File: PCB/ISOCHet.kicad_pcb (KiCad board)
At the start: 2 copper layers, 57.1 x 38.1 mm, 19 parts, among them J1 USB_C_Receptacle_USB2.0, J2 Conn_01x08_Pin, SW0 BOOT, SW1 TAB, SW2 ENTER, SW3 CAPS, SW4 CAPS_STEP1.5, SW5 CAPS_STEP1.25, U1 CH552G, U2 USBLC6-2P6

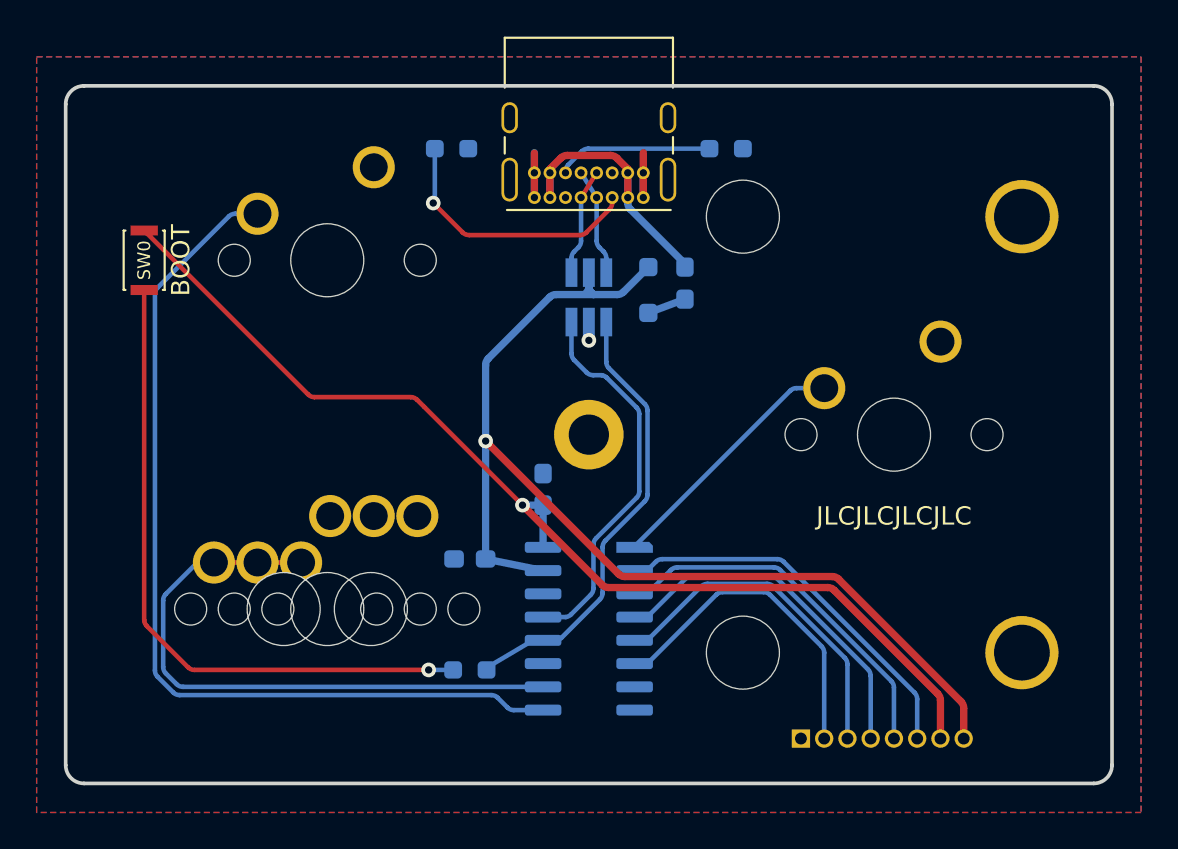
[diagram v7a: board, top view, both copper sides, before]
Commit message: Use larger footprint for J2 header
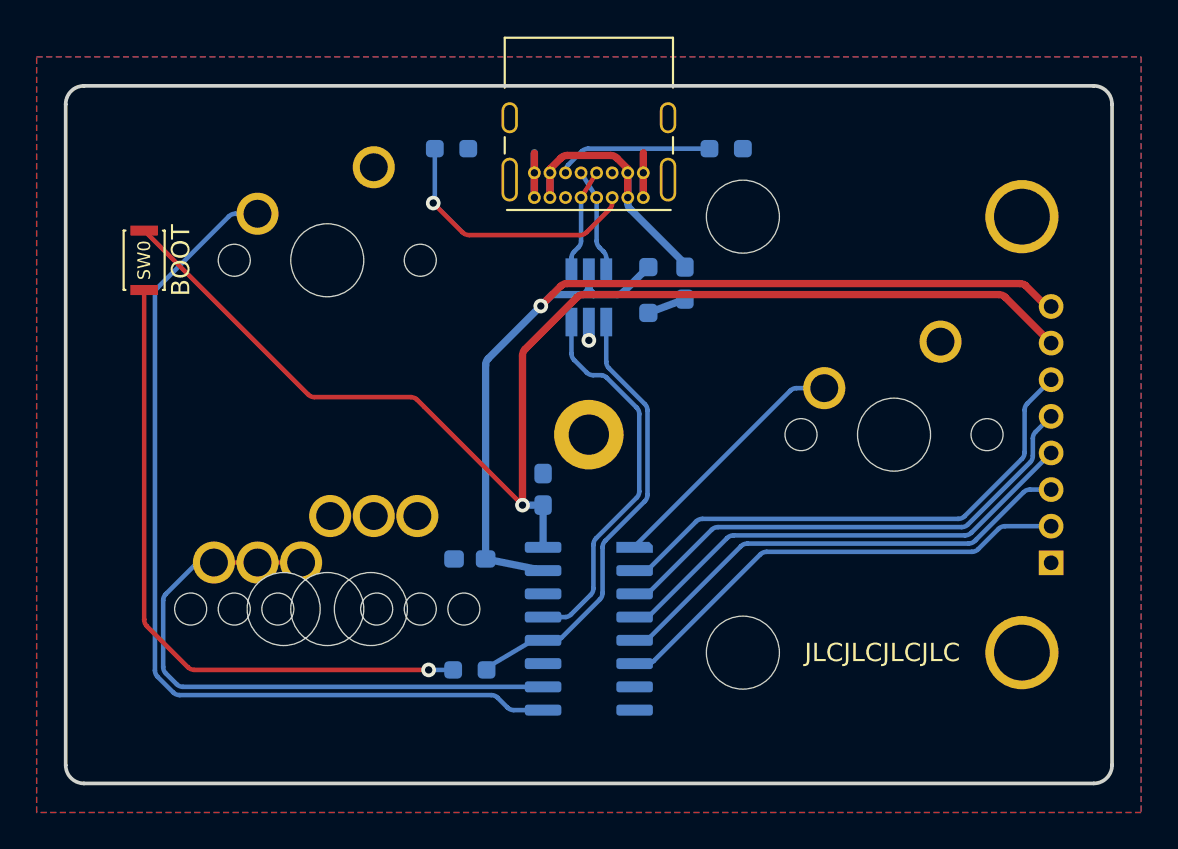
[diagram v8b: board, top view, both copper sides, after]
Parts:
- J2: footprint Connector_PinHeader_1.27mm:PinHeader_1x08_P1.27mm_Vertical -> Connector_PinHeader_2.00mm:PinHeader_1x08_P2.00mm_Vertical
- moved J2 16.7 mm to (184.0, 64.2), turned to 0 degrees
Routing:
- net +3V3: track 59.6 -> 69.8 mm
- net Net-(J2-Pin_2): track 18.1 -> 25.8 mm
- net Net-(J2-Pin_6): track 21.0 -> 28.5 mm
- net Net-(J2-Pin_3): track 18.8 -> 26.1 mm
- net Net-(J2-Pin_5): track 20.3 -> 27.4 mm
- net Net-(J2-Pin_4): track 19.5 -> 26.4 mm
- net VCC: track 61.2 -> 56.2 mm
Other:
- board text added: "1.4"
- board text added: "1.5"
- board text added: "1.6"
- board text added: "3.0"
- board text added: "3.1"
- board text removed: "P1.4"
- board text removed: "P1.5"
- board text removed: "P1.6"
- board text removed: "P3.0"
- board text removed: "P3.1"
